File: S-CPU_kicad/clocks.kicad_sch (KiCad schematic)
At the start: 137 parts

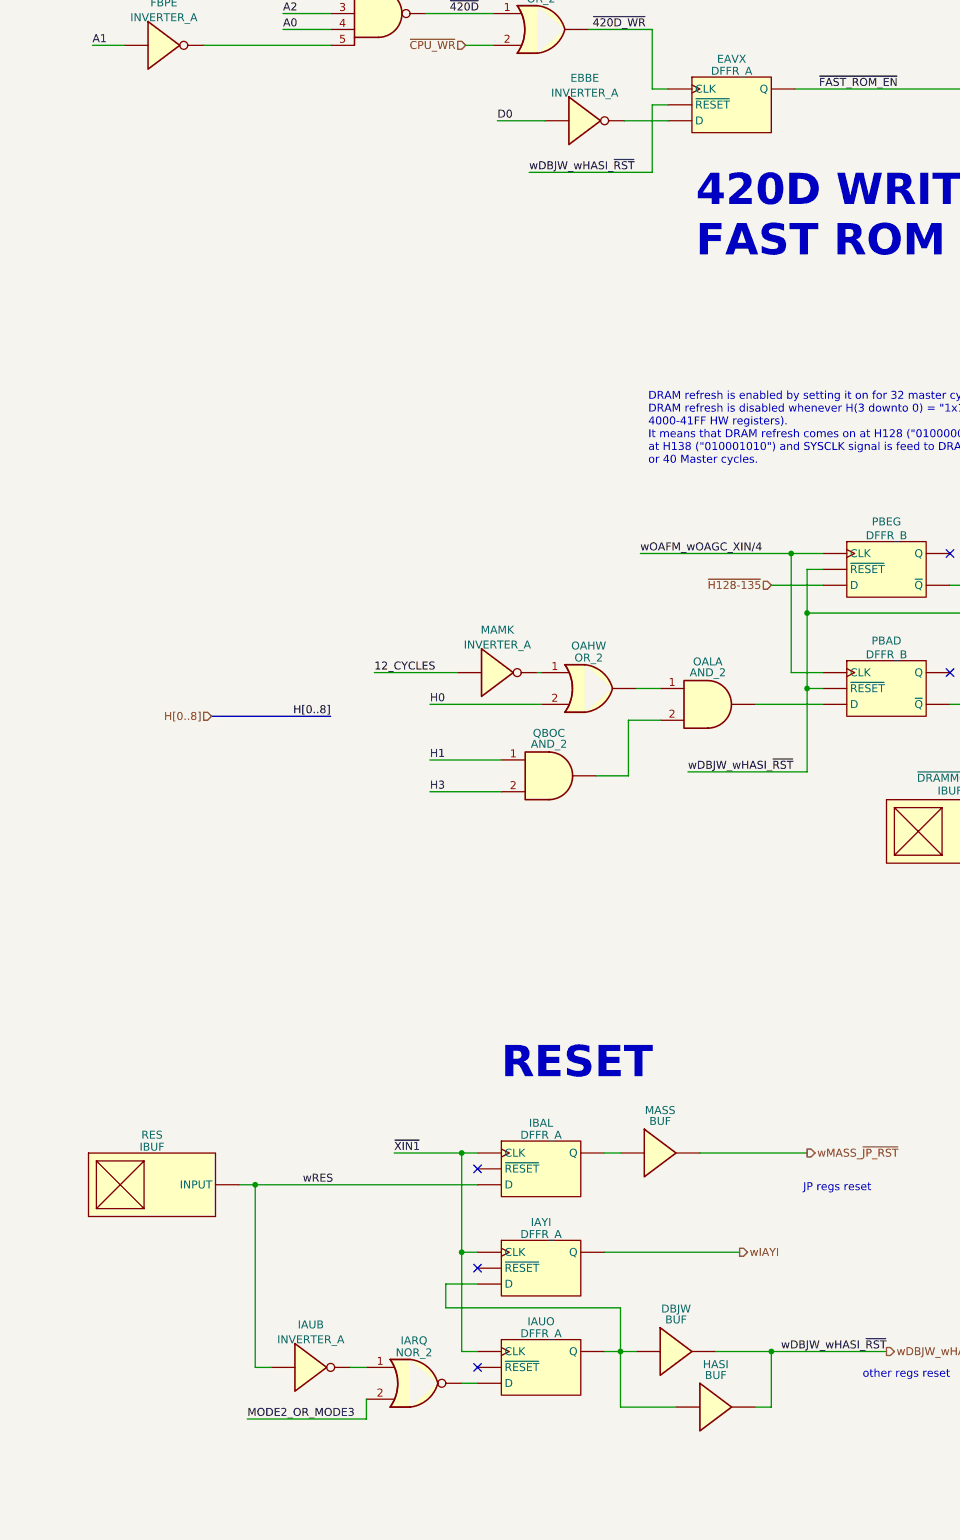
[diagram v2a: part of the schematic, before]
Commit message: Fix ERC errors in schematics.
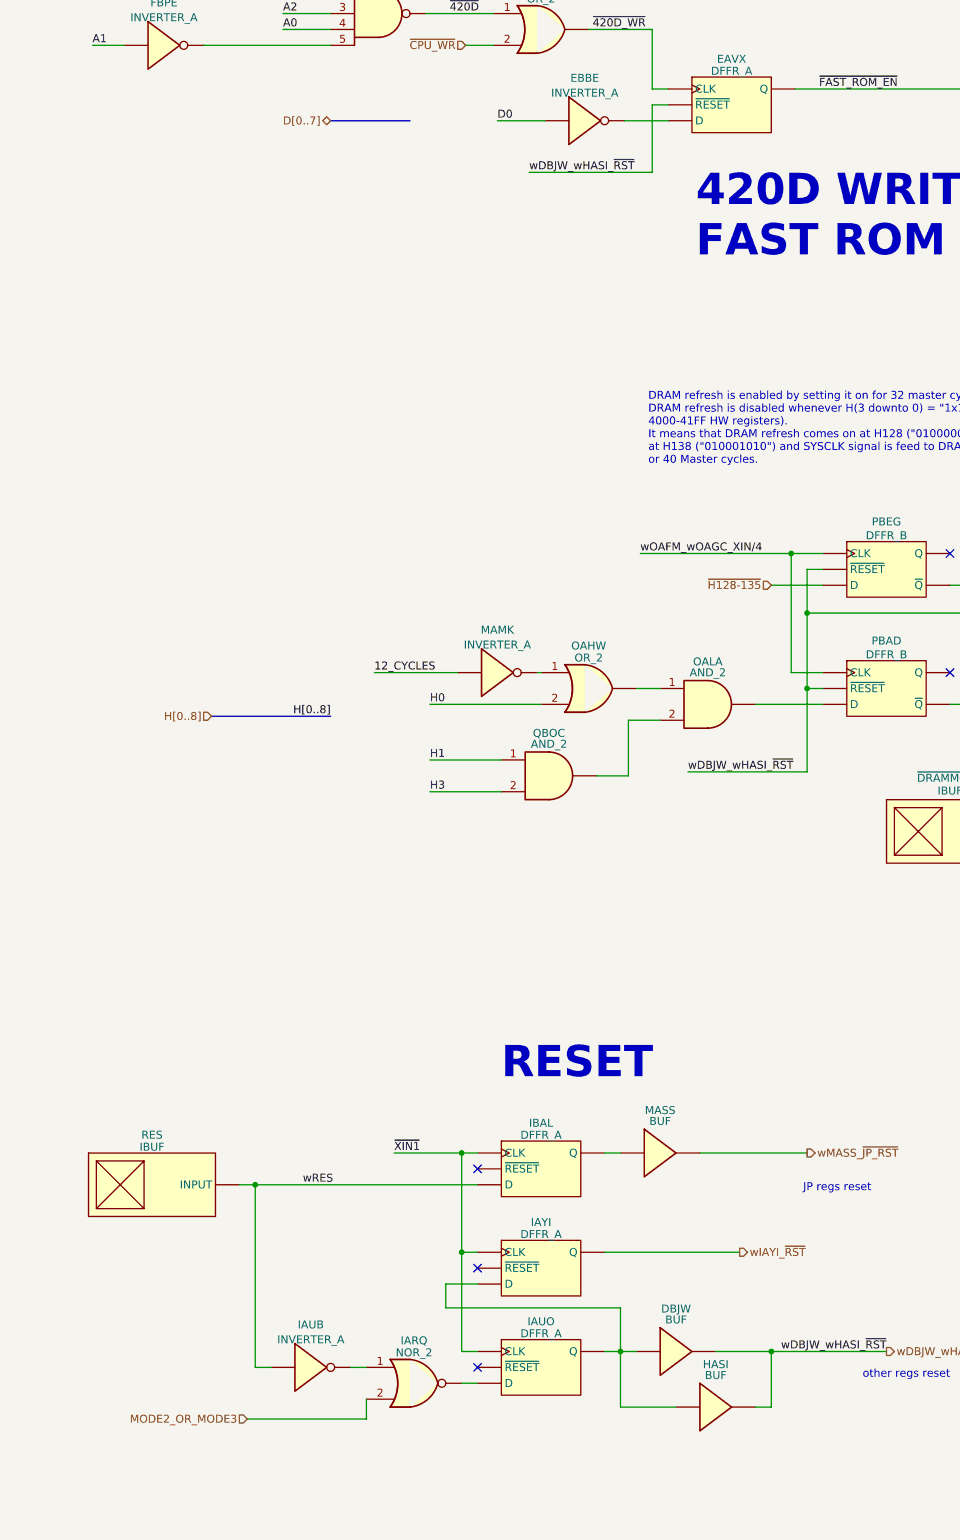
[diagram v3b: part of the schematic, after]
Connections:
- net wIAYI renamed wIAYI_~{RST}
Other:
- title: SNES S-CPU Schematics  -> Reverse Engineered SNES S-CPU Schematics 
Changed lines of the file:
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@@
   (paper "A1")
   (title_block
-    (title "SNES S-CPU Schematics ")
+    (title "Reverse Engineered SNES S-CPU Schematics ")
     (date "2023-10-21")
     (rev "0.1")
@@
     (stroke (width 0) (type default))
   )
+  (bus (pts (xy 171.45 177.8) (xy 184.15 177.8))
+    (stroke (width 0) (type default))
+  )
   (wire (pts (xy 493.395 354.33) (xy 493.395 410.21))
     (stroke (width 0) (type default))
@@
     (effects (font (size 1.27 1.27)) (justify left bottom))
   )
-  (label "MODE2_OR_MODE3" (at 158.115 385.445 0) (fields_autoplaced)
-    (effects (font (size 1.27 1.27)) (justify left bottom))
-  )
   (label "wKBIE" (at 490.22 118.745 180) (fields_autoplaced)
     (effects (font (size 1.27 1.27)) (justify right bottom))
@@
     (effects (font (size 1.27 1.27)) (justify right))
   )
+  (hierarchical_label "D[0..7]" (shape bidirectional) (at 171.45 177.8 180) (fields_autoplaced)
+    (effects (font (size 1.27 1.27)) (justify right))
+  )
   (hierarchical_label "MODE1_OR_MODE3" (shape input) (at 377.825 242.57 180) (fields_autoplaced)
     (effects (font (size 1.27 1.27)) (justify right))
@@
     (effects (font (size 1.27 1.27)) (justify left))
   )
-  (hierarchical_label "wIAYI" (shape output) (at 236.855 358.775 0) (fields_autoplaced)
+  (hierarchical_label "wIAYI_~{RST}" (shape output) (at 236.855 358.775 0) (fields_autoplaced)
     (effects (font (size 1.27 1.27)) (justify left))
   )
@@
     (effects (font (size 1.27 1.27)) (justify left))
   )
+  (hierarchical_label "MODE2_OR_MODE3" (shape input) (at 158.115 385.445 180) (fields_autoplaced)
+    (effects (font (size 1.27 1.27)) (justify right))
+  )
   (hierarchical_label "wMBLO_~{XIN{slash}256}" (shape output) (at 527.05 444.5 0) (fields_autoplaced)

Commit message: Big rework on the hierachical sheet to make thigs a bit clearer. PDF exported for Rev 0.1.
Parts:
- removed BAEW, BAFF: NOR_2, symbol Ricoh_Cells:NOR_2
- removed BANP, FBFE: OR_2, symbol Ricoh_Cells:OR_2
- removed BANW, BAYS, CAZC, EBBE, FBPE: INVERTER_A, symbol Ricoh_Cells:INVERTER_A
- removed BANX: NAND_2, symbol Ricoh_Cells:NAND_2
- removed BAOZ: NAND_4, symbol Ricoh_Cells:NAND_4
- removed BAPI: NAND_3, symbol Ricoh_Cells:NAND_3
- removed BBAR: AND_2, symbol Ricoh_Cells:AND_2
- removed CABL: OAI_112, symbol Ricoh_Cells:OAI_112
- removed CAZD: NOR_6, symbol Ricoh_Cells:NOR_6
- removed EAVX, JAOO, JAQD: DFFR_A, symbol Ricoh_Cells:DFFR_A
- removed FBII: NAND_5, symbol Ricoh_Cells:NAND_5
- removed HAUU0, HAUU1: MUX, symbol Ricoh_Cells:MUX
- removed IBNQ: DEMUX_2-3, symbol Ricoh_Cells:DEMUX_2-3
- removed TCKSEL0, TCKSEL1: IBUF, symbol Ricoh_Cells:IBUF
- added JBDJ: BUF, symbol Ricoh_Cells:BUF
- added JBHT: DFFR_A, symbol Ricoh_Cells:DFFR_A
- added LBWH, OAYK, WAJJ, WAOX: INVERTER_A, symbol Ricoh_Cells:INVERTER_A
- added OAXV: AND_2, symbol Ricoh_Cells:AND_2
- added WAMB: AOI_22, symbol Ricoh_Cells:AOI_22
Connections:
- net wNBHJ_wNBHM_XIN/2 is gone; now on net XIN/2: NBHJ.2, NBHM.2
- net wNBRL_wNBQA_~{XIN/4} is gone; now on net ~{XIN/4}: NBQA.2, NBRL.2
- net XIN: now also CAKS.1 (CLK), CAKW.1 (CLK), CANH.1 (CLK), CAQL.1 (CLK), CBDC.1 (CLK), CBEP.1 (CLK), CBFI.1 (CLK), CBGC.1 (CLK); no longer CAKS.3 (CLK), CAKS.4 (~{CLK}), CAKW.3 (CLK), CAKW.4 (~{CLK}), CANH.3 (CLK), CANH.4 (~{CLK}), CAQL.3 (CLK), CAQL.4 (~{CLK}), CBDC.3 (CLK), CBDC.4 (~{CLK}), CBEP.3 (CLK), CBEP.4 (~{CLK}), CBFI.3 (CLK), CBFI.4 (~{CLK}), CBGC.3 (CLK), CBGC.4 (~{CLK})
- net XIN/2: no longer NBCF.2, NBHJ.1, NBHM.1, NBWF.7 (Q)
- net XIN/4: now also ESQB.1 (CLK), OAFM.2, OAGC.2, PBAD.1 (CLK), PBEG.1 (CLK); no longer NAPZ.2, NBSM.7 (Q), OAFM.1, OAGC.1
- net wIAYI_~{RST}: now also IAYI.9 (Q), JBHT.6 (~{RESET}); no longer IAYI.6 (Q)
- net wKAVS: now also KAVS.9 (Q); no longer KAVS.6 (Q)
- net wKBGM: now also KBGM.9 (Q); no longer KBGM.6 (Q)
- net wKBIE: now also KBIE.9 (Q); no longer KBIE.6 (Q)
- net wKBKC: now also KBKC.9 (Q); no longer KBKC.6 (Q)
- net wKBLJ: now also JAFF.1 (CLK), KBLJ.9 (Q); no longer JAFF.3 (CLK), JAFF.4 (~{CLK}), KBLJ.6 (Q)
- net wMAOG: now also MAOG.9 (Q); no longer MAOG.7 (Q)
- net wMBFM_XIN/8: now also ESOJ.1 (CLK), MBFM.9 (Q); no longer ESOJ.3 (CLK), ESOJ.4 (~{CLK}), MBFM.7 (Q)
- net ~{XIN/4}: now also WAMB.1; no longer MBFM.3 (CLK), MBFM.4 (~{CLK}), MBLO.3 (CLK), MBLO.4 (~{CLK}), NBJW.2, NBQA.1, NBRL.1, NBSM.6 (~{Q})
- net ~{wMAOG}: now also MAOG.8 (~{Q}); no longer MAOG.6 (~{Q})
- net at BBNU.5, CAXW.3 (2): now also CAKW.8 (~{Q}); no longer CAKW.6 (~{Q})
- net at KBIE.2 (D): now also KBIF.9 (Q); no longer KBIF.6 (Q)
- net at BBHQ.3 (2), BBKY.3, BBNU.3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: now also CAQL.8 (~{Q}); no longer CAQL.6 (~{Q})
- net at BBNU.4, CAWC.3 (2), CAXV.4: now also CANH.8 (~{Q}); no longer CANH.6 (~{Q})
- net at PAWC.1 (SET): now also PBEG.8 (~{Q}); no longer PBEG.6 (~{Q})
- net ~{XIN}: now reaches NBWF.1 (CLK)
- net ~{XIN}: now also IAUO.1 (CLK), IAYI.1 (CLK), IBAL.1 (CLK), JAWP.2, KAVS.1 (CLK), KAYP.1 (CLK), KBGM.1 (CLK), KBGO.1 (CLK), KBIE.1 (CLK), KBIF.1 (CLK), KBKC.1 (CLK), KBLJ.1 (CLK), KBMV.1 (CLK); no longer NBWF.5 (~{RESET})
- net at NBWF.2 (D): now also CBGC.9 (Q); no longer CBGC.7 (Q)
- net at DBJW.1, HASI.1, IAYI.2 (D): now also IAUO.9 (Q); no longer IAUO.6 (Q)
- net at ESQB.2 (D): now also ESOJ.9 (Q); no longer ESOJ.6 (Q)
- net at MBLO.2 (D): now also CAKS.9 (Q); no longer CAKS.7 (Q)
- net at KBLJ.2 (D): now also KBMV.9 (Q); no longer KBMV.6 (Q)
- net at KAVS.2 (D): now also KAYP.9 (Q); no longer KAYP.6 (Q)
- net at KBGM.2 (D): now also KBGO.9 (Q); no longer KBGO.6 (Q)
- net at BBKM.2, BBKY.2, BBNU.2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: now also CBDC.8 (~{Q}); no longer CBDC.6 (~{Q})
- net at MAHR.1, MAJY.2: now also ESQB.9 (Q); no longer ESQB.6 (Q)
- net at JAGY.1: now also JAFF.9 (Q); no longer JAFF.6 (Q)
- net at AAXD.1, ACKS.1, BCGJ.2 (1)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: now also CBGC.8 (~{Q}); no longer CBGC.6 (~{Q})
- net at AAXD.2, ACKS.2, BCGJ.3 (2): now also CBFI.8 (~{Q}); no longer CBFI.6 (~{Q})
- net at BBFY.3 (2): now also CAKS.8 (~{Q}); no longer CAKS.6 (~{Q})
- net ~{wNBWF_XIN/2}: now reaches NBSM.1 (CLK)
- net ~{wNBWF_XIN/2}: now also NBUB.2, NBWF.8 (~{Q}); no longer NBSM.5 (~{RESET})
- net at NBSM.2 (D): now also CBFI.9 (Q); no longer CBFI.7 (Q)
- net at PAWH.2: now also PBAD.8 (~{Q}); no longer PBAD.6 (~{Q})
- net at AAVE.3 (2), ACKS.3: now also CBEP.8 (~{Q}); no longer CBEP.6 (~{Q})
- net at MBFM.2 (D): now also CBEP.9 (Q); no longer CBEP.7 (Q)
- net at MASS.1: now also IBAL.9 (Q); no longer IBAL.6 (Q)
- removed net wDBJW_wHASI_~{RST}: CAKS.1 (~{RESET}), CAKS.5 (~{RESET}), CAKW.1 (~{RESET}), CAKW.5 (~{RESET}), CANH.1 (~{RESET}), CANH.5 (~{RESET}), CAQL.1 (~{RESET}), CAQL.5 (~{RESET}), CBDC.1 (~{RESET}), CBDC.5 (~{RESET}), CBEP.1 (~{RESET}), CBEP.5 (~{RESET}), CBFI.1 (~{RESET}), CBFI.5 (~{RESET}), CBGC.1 (~{RESET}), CBGC.5 (~{RESET}), DBJW.2, ESOJ.1 (~{RESET}), ESOJ.5 (~{RESET}), ESQB.1 (~{RESET}), ESQB.5 (~{RESET}), HASI.2, JAFF.1 (~{RESET}), JAFF.5 (~{RESET}), KAEZ.1 (~{RESET}), KAEZ.5 (~{RESET}), KAVS.1 (~{RESET}), KAVS.5 (~{RESET}), KAYP.1 (~{RESET}), KAYP.5 (~{RESET}), KBGM.1 (~{RESET}), KBGM.5 (~{RESET}), KBGO.1 (~{RESET}), KBGO.5 (~{RESET}), KBIE.1 (~{RESET}), KBIE.5 (~{RESET}), KBIF.1 (~{RESET}), KBIF.5 (~{RESET}), KBKC.1 (~{RESET}), KBKC.5 (~{RESET}), KBLJ.1 (~{RESET}), KBLJ.5 (~{RESET}), KBMV.1 (~{RESET}), KBMV.5 (~{RESET}), MAOG.1 (~{RESET}), MAOG.5 (~{RESET}), MBFM.1 (~{RESET}), MBFM.5 (~{RESET}), MBLO.1 (~{RESET}), MBLO.5 (~{RESET}), PAWH.1, PBAD.1 (~{RESET}), PBAD.5 (~{RESET}), PBEG.1 (~{RESET}), PBEG.5 (~{RESET})
- net wKAEZ renamed CPU_REFRESH_EN
- net CPU_REFRESH_EN: now also KAEZ.9 (Q); no longer KAEZ.6 (Q)
- net wMAGR_wMAGV renamed DMA_SYSCLK
- net wMASS_~{JP_RST} renamed ~{JP_RST}
- net wMBLO_~{XIN/256}: no longer names the net of OATI.1
- net wMBLO_~{XIN/256}: now also MBLO.8 (~{Q}), LBWH.1; no longer MBLO.6 (~{Q})
- net wNAGK_wNAJD renamed ~{DMA_SYSCLK}
- net wNAQE_wNBBM_XIN/2 renamed DMA_XIN/2
- net wNBEB_wNBEG_XIN/8 renamed DMA_XIN/8
- net wNBKW_wNBPG_~{XIN/4} renamed DMA_~{XIN/4}
- net wOACU_wOAFI_XIN/4 renamed DMA_XIN/4
- removed net wOAFM_wOAGC_XIN/4: ESQB.3 (CLK), ESQB.4 (~{CLK}), OAFM.2, OAGC.2, PBAD.3 (CLK), PBAD.4 (~{CLK}), PBEG.3 (CLK), PBEG.4 (~{CLK})
- net wOAGE_SYSCLK renamed MULDIV_SYSCLK
- net wOATI_~{XIN/256} renamed ~{XIN/256}
- net ~{XIN/256}: now also WAMB.3
- net wOBXZ_wOCHV_~{XIN/2} renamed DMA_~{XIN/2}
- net wOCRQ_wOCRS_~{XIN/8} renamed DMA_~{XIN/8}
- removed net ~{XIN1}: IAUO.3 (CLK), IAUO.4 (~{CLK}), IAYI.3 (CLK), IAYI.4 (~{CLK}), IBAL.3 (CLK), IBAL.4 (~{CLK}), JAWP.2, KAVS.3 (CLK), KAVS.4 (~{CLK}), KAYP.3 (CLK), KAYP.4 (~{CLK}), KBGM.3 (CLK), KBGM.4 (~{CLK}), KBGO.3 (CLK), KBGO.4 (~{CLK}), KBIE.3 (CLK), KBIE.4 (~{CLK}), KBIF.3 (CLK), KBIF.4 (~{CLK}), KBKC.3 (CLK), KBKC.4 (~{CLK}), KBLJ.3 (CLK), KBLJ.4 (~{CLK}), KBMV.3 (CLK), KBMV.4 (~{CLK}), NBWF.3 (CLK), NBWF.4 (~{CLK})
- removed net ~{XIN/2}: NBSM.3 (CLK), NBSM.4 (~{CLK}), NBUB.2, NBWF.6 (~{Q})
- removed net ~{wMBFM}_~{XIN/8}: MAOG.3 (CLK), MAOG.4 (~{CLK}), MBDX.1, MBFM.6 (~{Q})
- new net: WAMB.3, WAOX.1
- new net: KAAQ.2, KAEZ.1 (CLK)
- new net: WAJJ.2, WAMB.4
- new net: JBHT.1 (CLK), LBWH.2
- new net: JBDJ.1, JBHT.9 (Q)
- new net: OAXV.2, OAYK.2
- new net +5V: JBHT.2 (D)
- new net COUNTER_TEST_MODE: OAXV.3, WAJJ.1, WAMB.2
- new net JP_CLK: WAOX.2
- new net wNBSM_XIN/4: NAPZ.2, NBSM.9 (Q), OAFM.1, OAGC.1
- new net wNBWF_XIN/2: NBCF.2, NBHJ.1, NBHM.1, NBWF.9 (Q)
- new net ~{CPU_RST}: JBDJ.2
- new net ~{MODE6}: OAYK.1
- new net ~{MRST}: CAKS.6 (~{RESET}), CAKW.6 (~{RESET}), CANH.6 (~{RESET}), CAQL.6 (~{RESET}), CBDC.6 (~{RESET}), CBEP.6 (~{RESET}), CBFI.6 (~{RESET}), CBGC.6 (~{RESET}), DBJW.2, ESOJ.6 (~{RESET}), ESQB.6 (~{RESET}), HASI.2, JAFF.6 (~{RESET}), KAEZ.6 (~{RESET}), KAVS.6 (~{RESET}), KAYP.6 (~{RESET}), KBGM.6 (~{RESET}), KBGO.6 (~{RESET}), KBIE.6 (~{RESET}), KBIF.6 (~{RESET}), KBKC.6 (~{RESET}), KBLJ.6 (~{RESET}), KBMV.6 (~{RESET}), MAOG.6 (~{RESET}), MBFM.6 (~{RESET}), MBLO.6 (~{RESET}), PAWH.1, PBAD.6 (~{RESET}), PBEG.6 (~{RESET})
- new net ~{wMBFM_XIN/8}: MAOG.1 (CLK), MBDX.1, MBFM.8 (~{Q})
- new net ~{wNBSM_XIN/4}: MBFM.1 (CLK), MBLO.1 (CLK), NBJW.2, NBQA.1, NBRL.1, NBSM.8 (~{Q})
- new net ~{wRDY}: OAXV.1
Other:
- note added: "Normal clock is XIN/256 which will take 3 scamline lines to fill in jp shift registers. In MODE6, XIN/4 clock is used instead when RDY = 0."
- note removed: "420D WRITE FAST ROM ENABLE"
- note removed: "IO range: x0xx xxxx 0xxx xxxx xxxx xxxx"
- note removed: "~{0000-1FFF} is WRAM ~{6000-7FFF} is expansion ~{4000-41FF} is controller 0000-7FFF is IO range BOAZ is low when accessing 2000-3FFF range (PPU, APU) and 4200-5FFF range (CPU + DMA) BANP is low when A23 is high but not in IO range i.e. FAST ROM access Therefore CABL will be high to allow 6 master cycles per cpu cycle when CPU accesses fast rom, some IO registers and during internal cycles (provid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"
- moved on the sheet: DBJW, HASI, IARQ, IAUB, MASS, OATI, RES

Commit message: Fixed VAWR which should have been an SR DFF (to fix issue #3 raised in github)
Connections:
- net at WAOX.1: now also WAMB.5; no longer WAMB.3
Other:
- moved on the sheet: AAVE, AAXD, ACKS, ACLK, BBFY, BBHQ, BBKM, BBKY, BBNU, BCGJ, CAKS, CAKW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
